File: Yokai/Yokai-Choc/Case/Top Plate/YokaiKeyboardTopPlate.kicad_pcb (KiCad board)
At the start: 2 copper layers, 160.3 x 114.7 mm, 6 parts

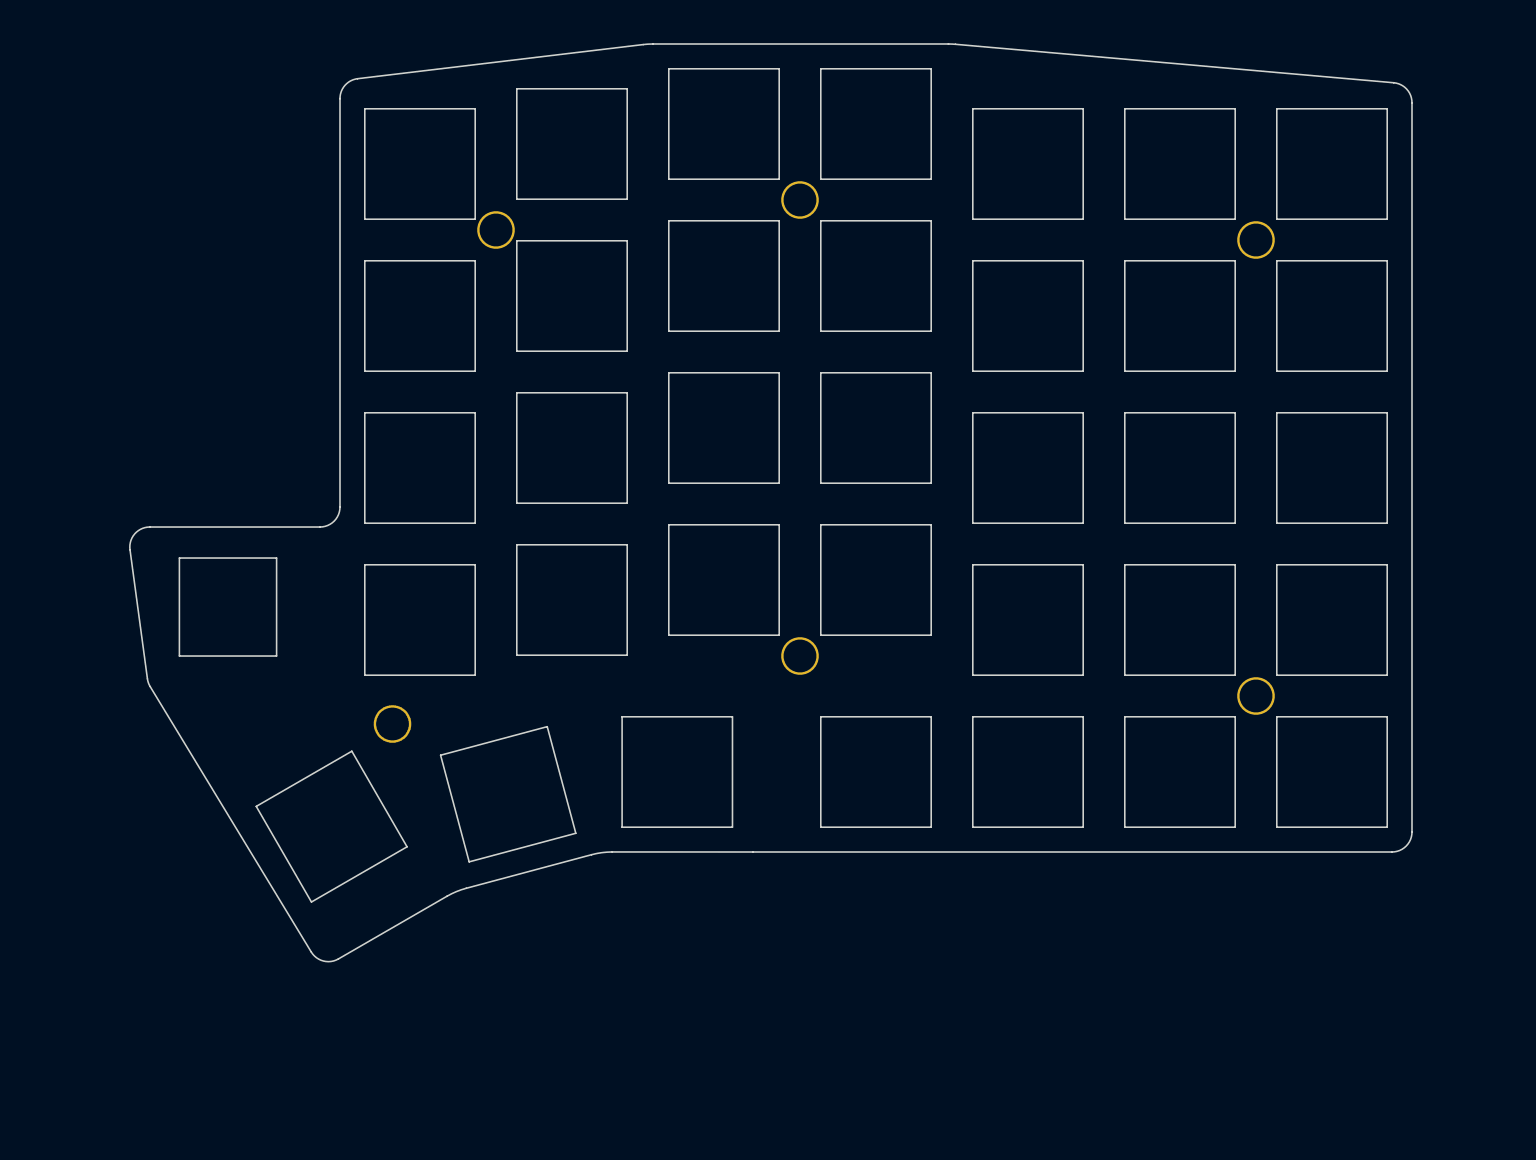
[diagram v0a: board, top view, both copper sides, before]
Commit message: Add files via upload
*Increased pinky stagger
*Inverted stabilizer cutouts
*Added additional thumb key
*Minor footprint changes
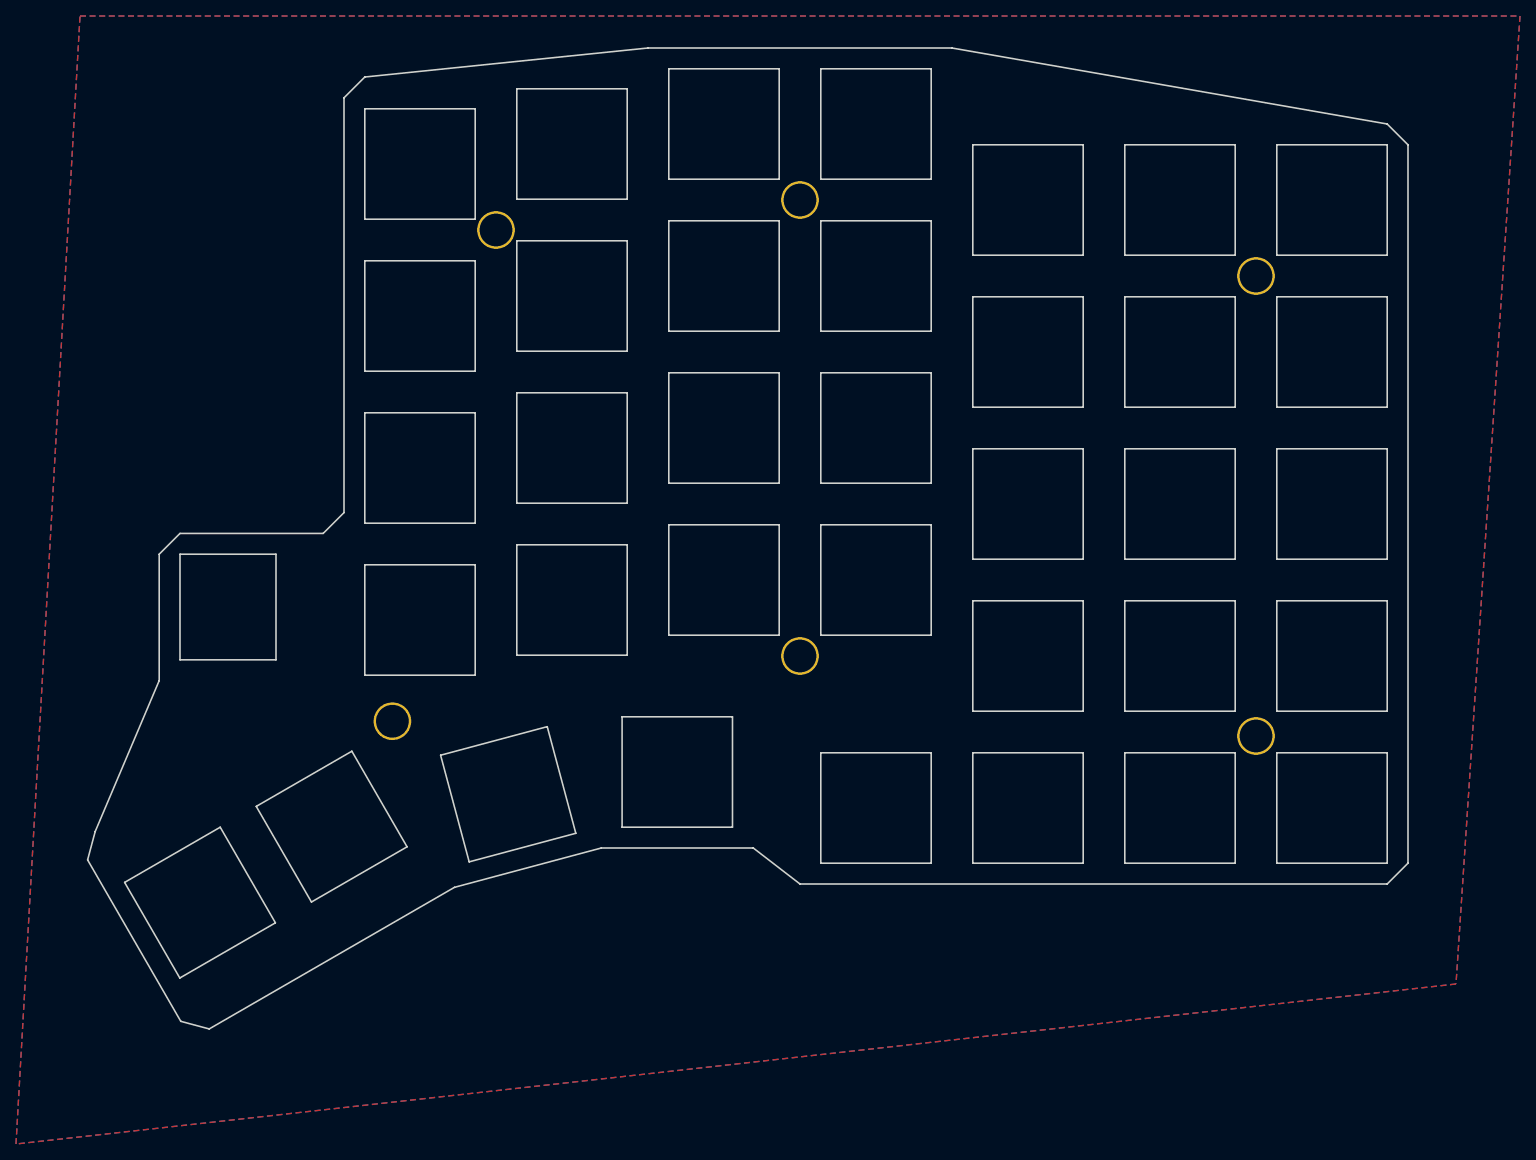
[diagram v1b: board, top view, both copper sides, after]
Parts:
- removed the TH5 at (113.1, 119.5)
- removed the TH5 at (221.0, 116.0)
- added TH5: HOLE, kbd:HOLE_M2_TH, F.Cu at (113.1, 119.2)
- added TH5: HOLE, kbd:HOLE_M2_TH, F.Cu at (221.0, 121.0)
- moved TH5 4.50 mm to (221.0, 63.5)
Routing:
- added copper zone on B.Cu, net (none)
- added copper zone on F.Cu, net (none)
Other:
- board size 160.3 x 114.7 mm -> 165.1 x 122.6 mm
